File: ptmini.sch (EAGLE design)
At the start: 47 parts, among them J4 MINI-USB-UX60A-MB-5ST, Q1 MMBT2222A, U1 MCP1703DB, U2 CY8C4248AZI-L485, U3 UBLOX_MAX, U4 MS5611-01BA03, U5 EEPROM-I2CSMD, U6 DRA818V, U7 PUSBM12VX4-TL-115

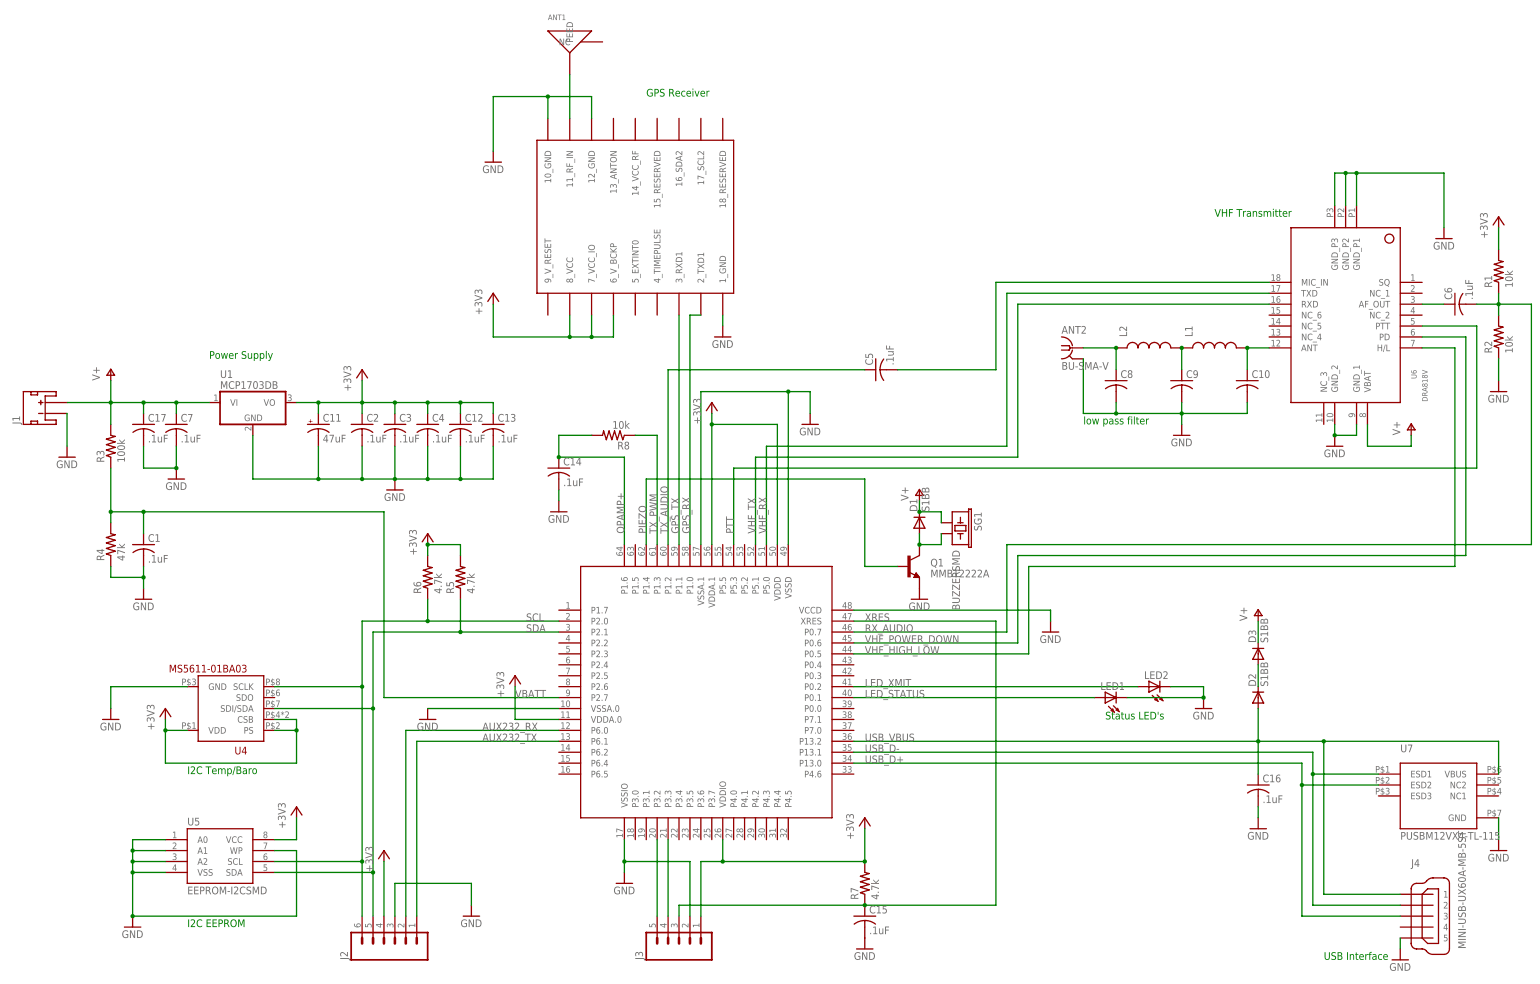
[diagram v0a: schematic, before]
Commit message: Board version 1.01.
Minor changes to a few of the component libraries.  Swapped out the
diodes with a smaller LL4148 diode.  Defined all component values and
Digikey part numbers.  Set values for low pass filter.  Renumbered board
to 1.01 to reflect the slight layout changes.  All components remain
unchanged otherwise.
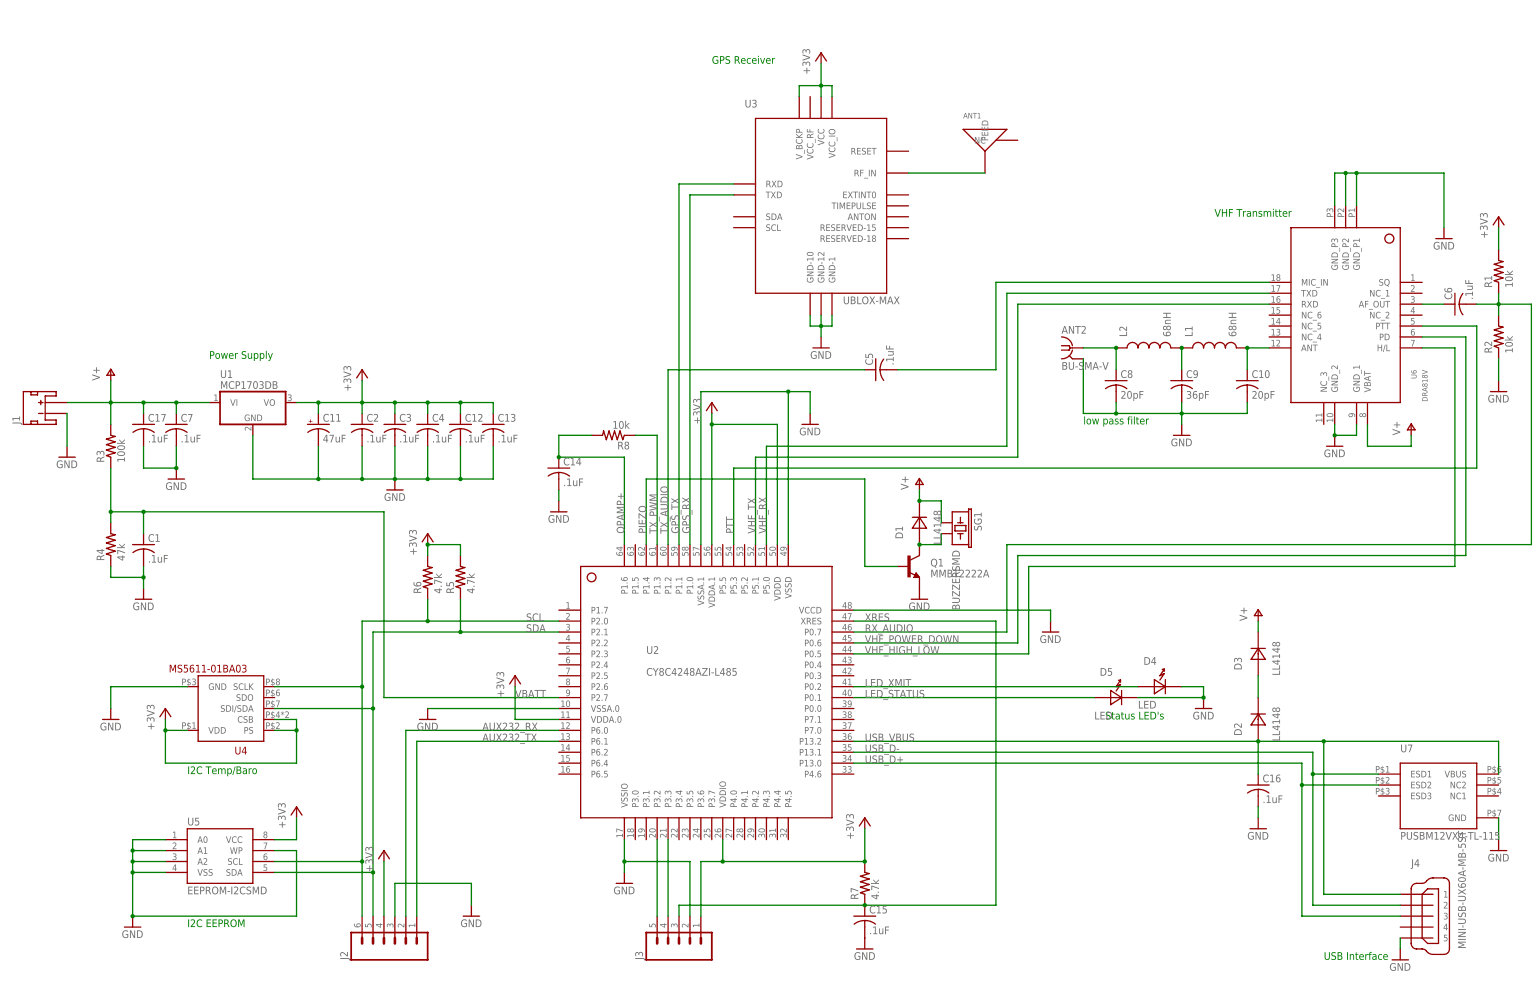
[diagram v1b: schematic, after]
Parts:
- removed LED1, LED2: (no value), eagle-ltspice:LED_E
- added D4, D5: LED, custom-ds:LED
- ANT2: DIGIKEY (none) -> CONSMA001-ND
- C1: DIGIKEY (none) -> 311-1361-1-ND
- C10, C8: value (none) -> 20pF; DIGIKEY (none) -> 712-1381-1-ND
- C9: value (none) -> 36pF; DIGIKEY (none) -> 712-1387-1-ND
- D1, D2, D3: value S1BB -> LL4148; device diode:DIODE-SMB -> custom-ds:LL4148; DIGIKEY S1BB-FDICT-ND -> (none)
- J2: DIGIKEY (none) -> WM4304-ND
- J3: DIGIKEY (none) -> SAM1112-32-ND
- L1: value (none) -> 68nH; DIGIKEY (none) -> 535-11572-2-ND OR AISC-0805-R068G-TCT-ND
- L2: value (none) -> 68nH
- R3: DIGIKEY (none) -> 311-100KCRCT-ND
- R4: DIGIKEY (none) -> 311-47.0KCRCT-ND
- U3: value UBLOX_MAX -> UBLOX-MAX; device Ava:UBLOX_MAX -> custom-ds:UBLOX-MAX
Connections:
- removed net N$19: ANT1.FEED, U3.11_RF_IN
- removed net N$3: D2.C, D3.A
- new net N$4: ANT1.FEED, U3.RF_IN
- new net N$5: D2.CATHODE, D3.ANODE
- net +3V3: now also U3.VCC, U3.VCC_IO, U3.V_BCKP; no longer U3.6_V_BCKP, U3.7_VCC_IO, U3.8_VCC
- net GND: now also D4.CATHODE, D5.CATHODE, U3.GND-1, U3.GND-10, U3.GND-12; no longer LED1.C, LED2.C, U3.10_GND, U3.12_GND, U3.1_GND
- net GPS_RX: now also U3.TXD; no longer U3.2_TXD1
- net GPS_TX: now also U3.RXD; no longer U3.3_RXD1
- net LED_STATUS: now also D5.ANODE; no longer LED1.A
- net LED_XMIT: now also D4.ANODE; no longer LED2.A
- net N$1: now also D1.ANODE; no longer D1.A
- net USB_VBUS: now also D2.ANODE; no longer D2.A
- net V+: now also D1.CATHODE, D3.CATHODE; no longer D1.C, D3.C
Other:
- moved on the sheet: ANT1

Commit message: Board version 1.1.0
Fixed incorrect chip footprint for PSoC chip, and also a bad power
connection to the chip.  Relocated the piezo to the back side of the PCB
and consolidated down to 5cm x 6cm.
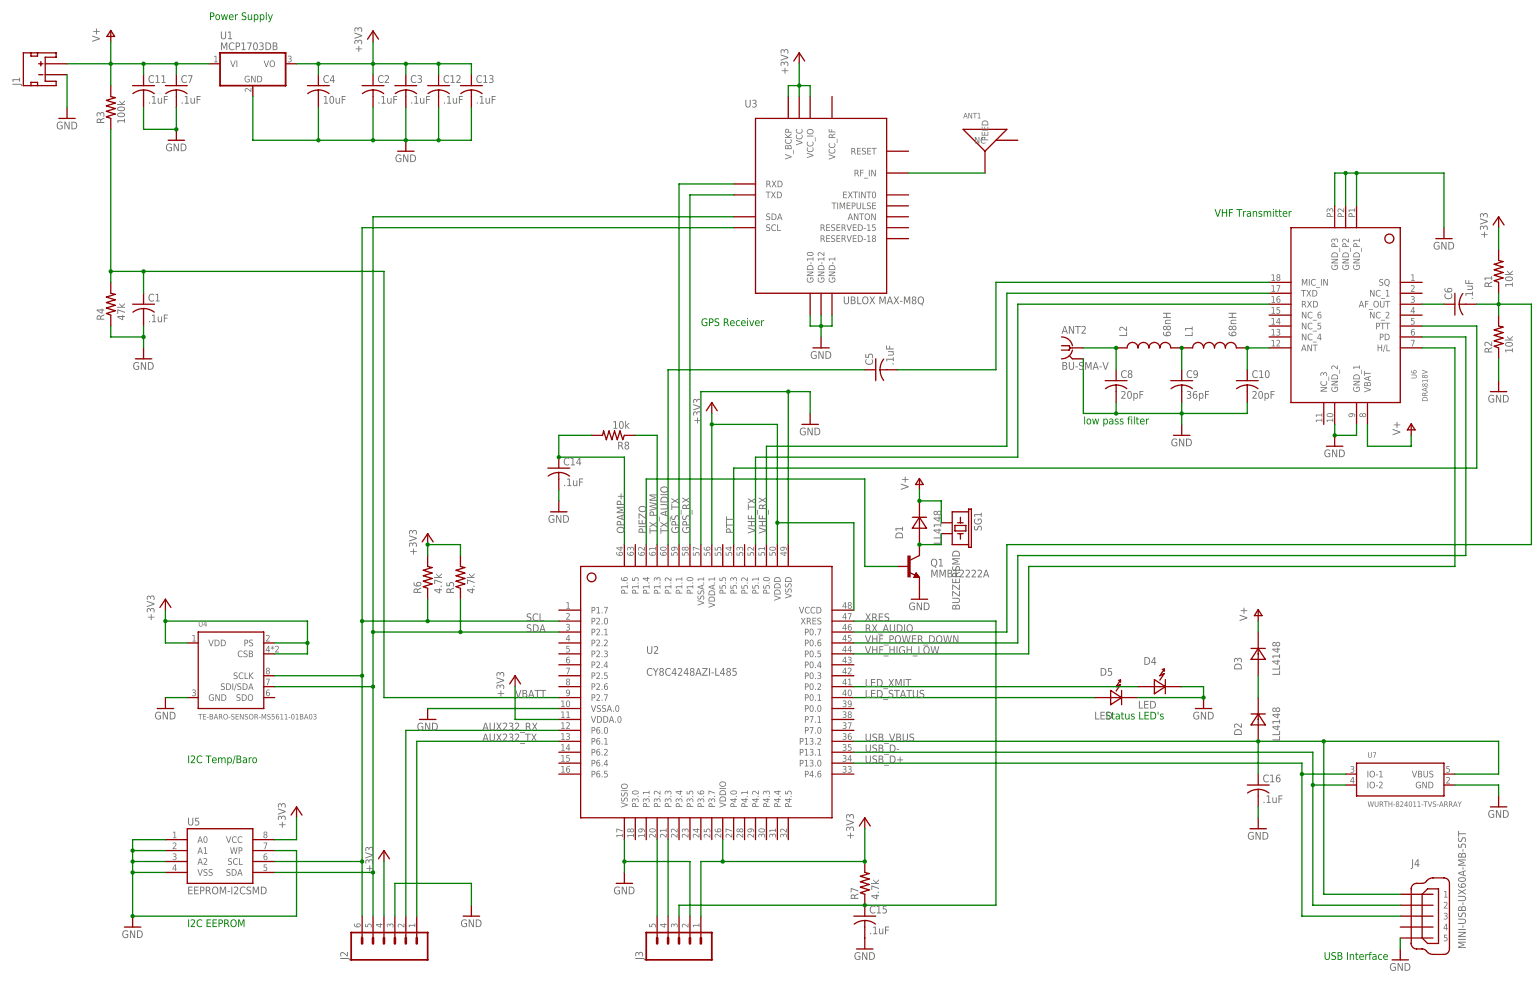
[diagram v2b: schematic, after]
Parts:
- removed C17: .1uF, resistor:C-USC0805
- C11: value 47uF -> .1uF; device resistor:CPOL-US153CLV-0605 -> resistor:C-USC0805; DIGIKEY PCE3842CT-ND -> 311-1361-1-ND
- C4: value .1uF -> 10uF; DIGIKEY 311-1361-1-ND -> 490-3886-1-ND
- D1, D2, D3: DIGIKEY (none) -> 568-1749-1-ND
- L1: DIGIKEY 535-11572-2-ND OR AISC-0805-R068G-TCT-ND -> AISC-0805-R068G-TCT-ND
- L2: DIGIKEY (none) -> AISC-0805-R068G-TCT-ND
- U3: value UBLOX-MAX -> UBLOX MAX-M8Q
- U4: value MS5611-01BA03 -> TE-BARO-SENSOR-MS5611-01BA03; device TE Connectivity Baro Sensor:MS5611-01BA03 -> custom-ds:TE-BARO-SENSOR-MS5611-01BA03
- U7: value PUSBM12VX4-TL-115 -> WURTH-824011-TVS-ARRAY; device custom-ds:PUSBM12VX4-TL-115 -> custom-ds:WURTH-824011-TVS-ARRAY; DIGIKEY 568-10918-1-ND -> 732-4465-1-ND
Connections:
- net +3V3: now also U2.VCCD; no longer C11.+
- net GND: now also C11.2; no longer C11.-, C17.2, U2.VCCD
- net SCL: now also U3.SCL
- net SDA: now also U3.SDA
- net USB_D+: now also U7.IO-1; no longer U7.ESD2
- net USB_D-: now also U7.IO-2; no longer U7.ESD1
- net V+: now also C11.1; no longer C17.1
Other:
- moved on the sheet: C1, C12, C13, C2, C3, C4, C7, J1, R3, R4, U1, U4
